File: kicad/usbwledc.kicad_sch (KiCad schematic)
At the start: 26 parts, among them J1 5V PAD, J10 USB_C_Receptacle_USB2.0, J2 D1 PAD, J3 GND PAD, J4 5V PAD, J5 D2 PAD, J6 GND PAD, J7 Accessories, SW1 FLASH_SW, U1 CH340N, U2 AMS1117-3.3, U3 ESP32-WROOM-32

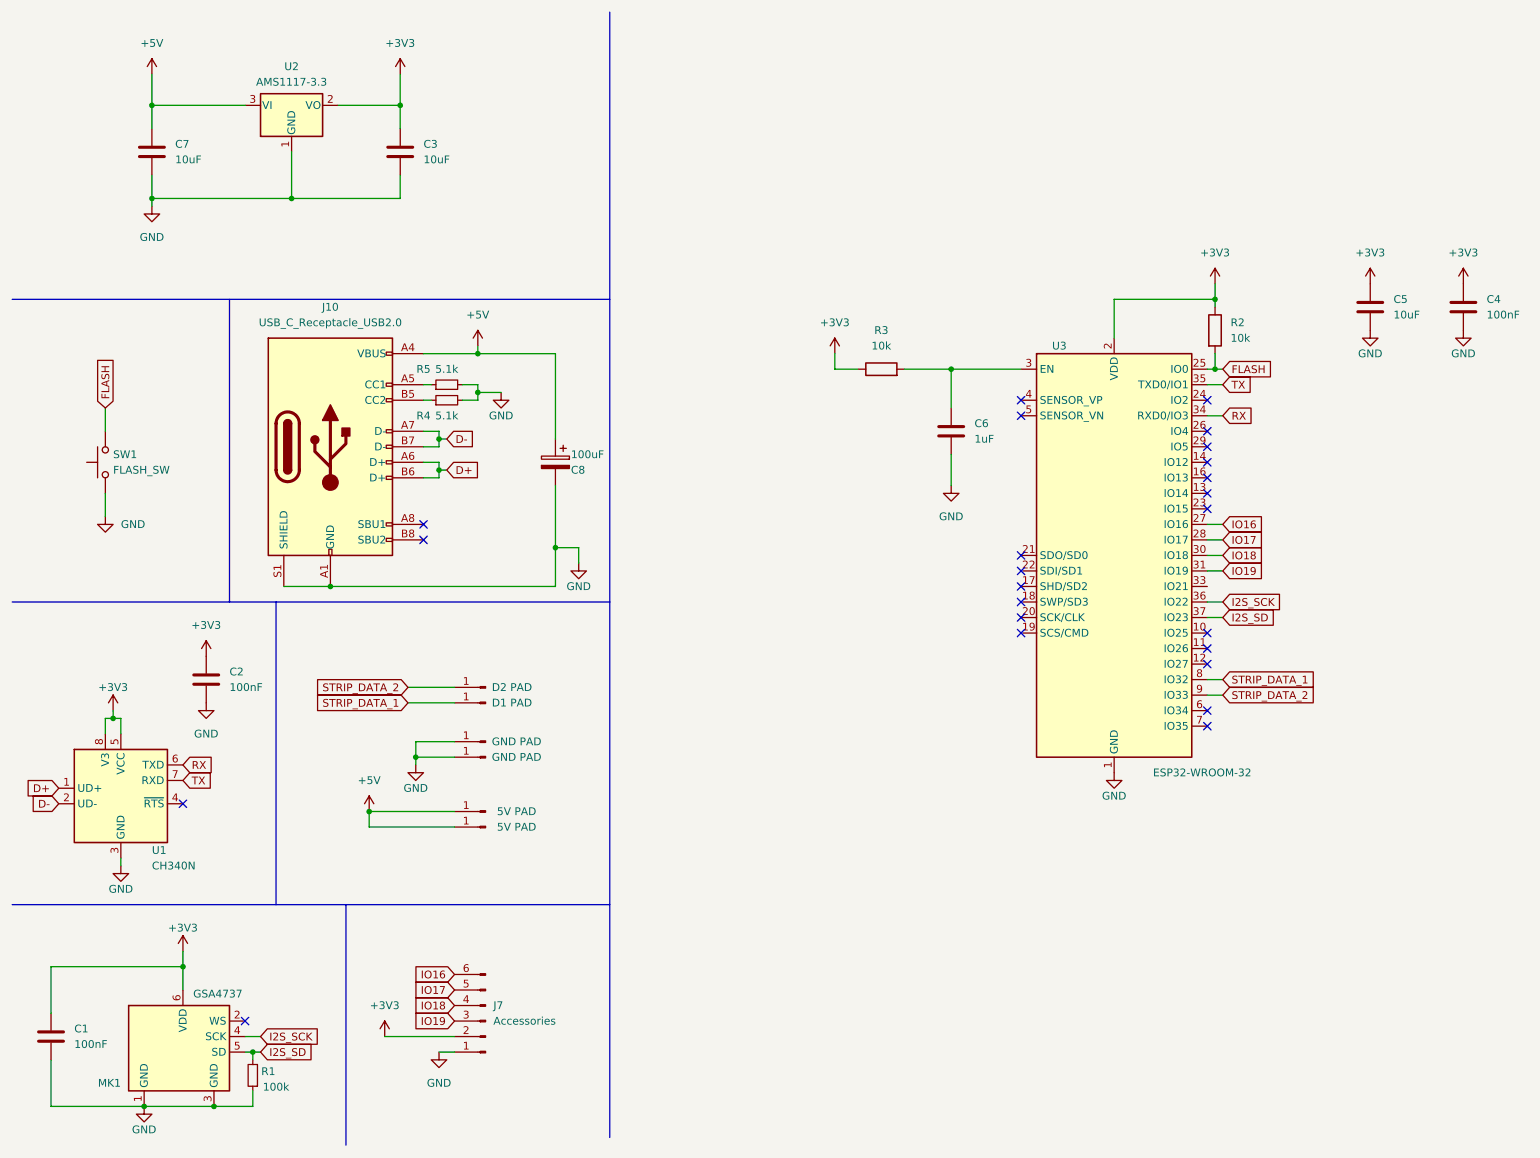
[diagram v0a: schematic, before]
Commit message: Replaced MEMS mic to a curent available version.
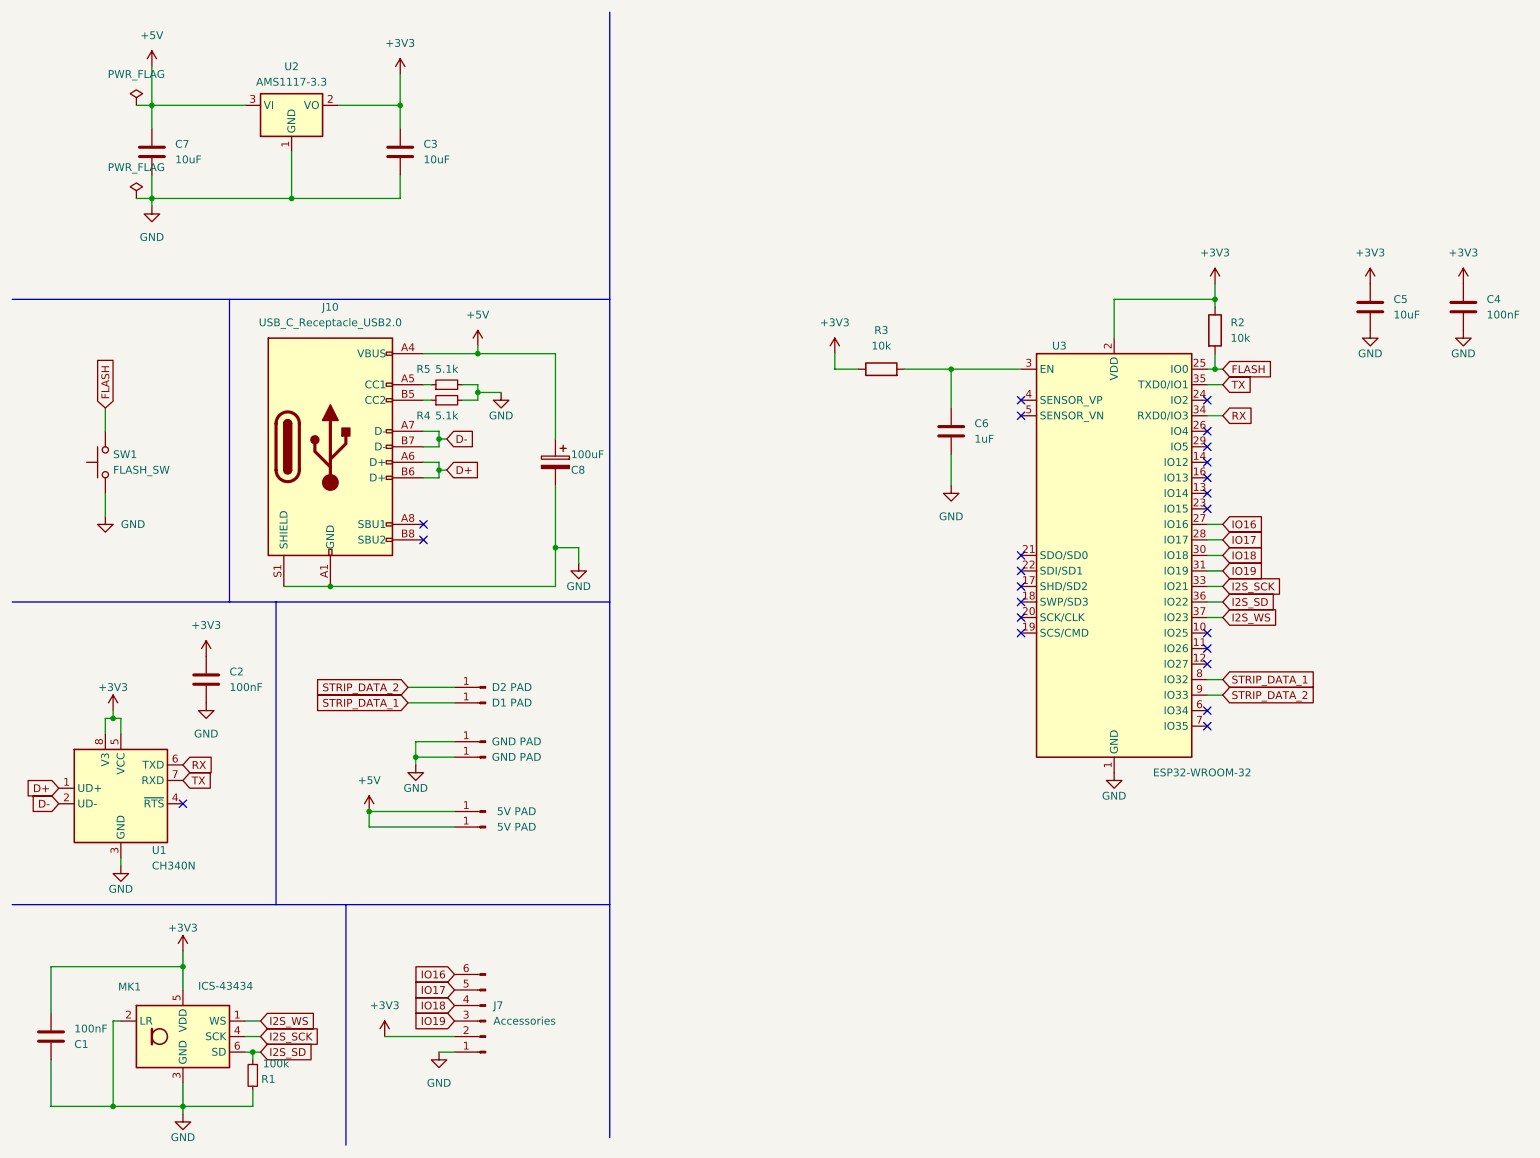
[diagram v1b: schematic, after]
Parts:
- C1, C2, C4: LCSC (none) -> C14663
- C3, C5, C7: LCSC (none) -> C15850
- C6: LCSC (none) -> C15849
- C8: LCSC (none) -> C96182
- J10: LCSC (none) -> C2988369
- MK1: value GSA4737 -> ICS-43434; footprint microphone:Microphone-6pin -> Sensor_Audio:InvenSense_ICS-43434-6_3.5x2.65mm; symbol microphone:GSA4737 -> Sensor_Audio:ICS-43434; LCSC (none) -> C5656610; MPN C5142171 -> (none)
- R1: LCSC (none) -> C25803
- R2, R3: LCSC (none) -> C25804
- R4, R5: LCSC (none) -> C23186
- SW1: LCSC (none) -> C318884
- U1: LCSC (none) -> C2977777
- U2: LCSC (none) -> C6186
- U3: LCSC (none) -> C701341
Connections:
- net +3V3: now also C1.2, MK1.5 (VDD); no longer C1.1, MK1.6 (VDD)
- net GND: now also C1.1, MK1.2 (LR), R1.2; no longer C1.2, MK1.1 (GND), R1.1
- net I2S_SCK: now also U3.33 (IO21); no longer U3.36 (IO22)
- net I2S_SD: now also MK1.6 (SD), R1.1, U3.36 (IO22); no longer MK1.5 (SD), R1.2, U3.37 (IO23)
- new net I2S_WS: MK1.1 (WS), U3.37 (IO23)
- no-connect marks 24 -> 23
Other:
- company: NANDXOR -> Adi Linden
- moved on the sheet: R1
